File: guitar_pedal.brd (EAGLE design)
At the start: 100 x 80 mm, 89 parts, among them P1 RM-065, P2 RM-065, P3 RM-065, U1 LM324N, U2 LM324N, U3 LM386N-3, U4 LM386N-3, U5 LM386N-3

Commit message: Finished organizing sheets
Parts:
- moved R18 63.5 mm to (-80.0, 48.3)
- moved JP10 62.7 mm to (-20.3, 78.7)
- moved JP4 60.0 mm to (-17.8, 83.8)
- moved R22 48.9 mm to (-26.7, 61.0)
- moved R23 48.9 mm to (-31.8, 61.0)
- moved R20 48.9 mm to (-16.5, 61.0)
- moved R21 48.9 mm to (-21.6, 61.0)
- moved C13 44.5 mm to (-16.5, 48.3)
- moved C16 44.5 mm to (-22.9, 48.3)
- moved C21 44.5 mm to (-35.6, 48.3)
- moved C19 44.5 mm to (-29.2, 48.3)
- moved R3 41.3 mm to (-31.8, 67.3)
- moved R4 41.3 mm to (-36.8, 67.3)
- moved U3 40.6 mm to (-71.1, 6.35)
- moved U1 40.2 mm to (-34.3, 6.35)
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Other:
- board size 100 x 80 mm -> 160 x 100 mm

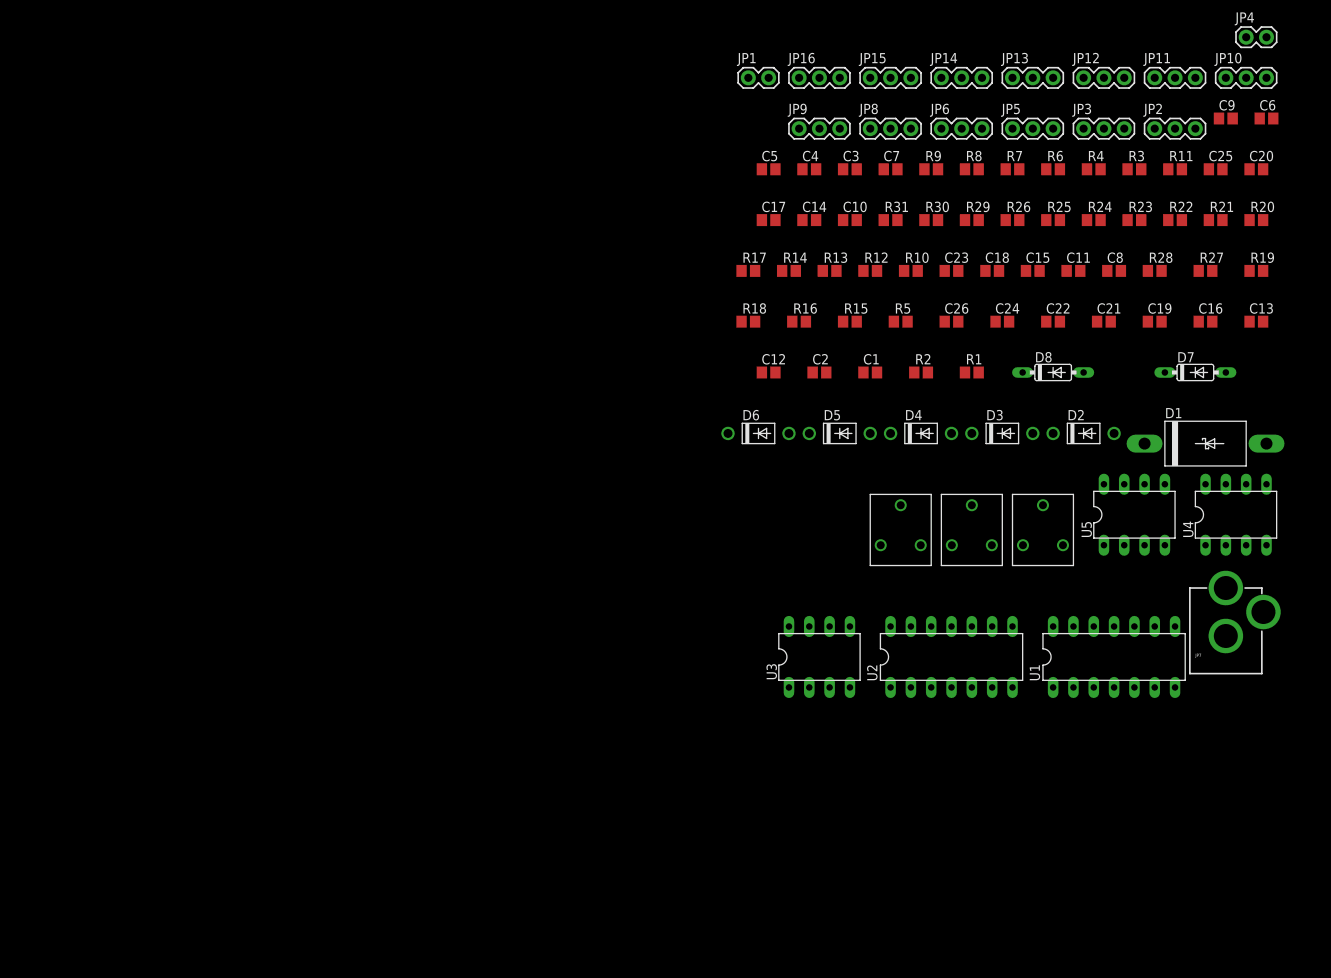
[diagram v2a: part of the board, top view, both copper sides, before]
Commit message: editted schematic to orgainize and fix mistakes.
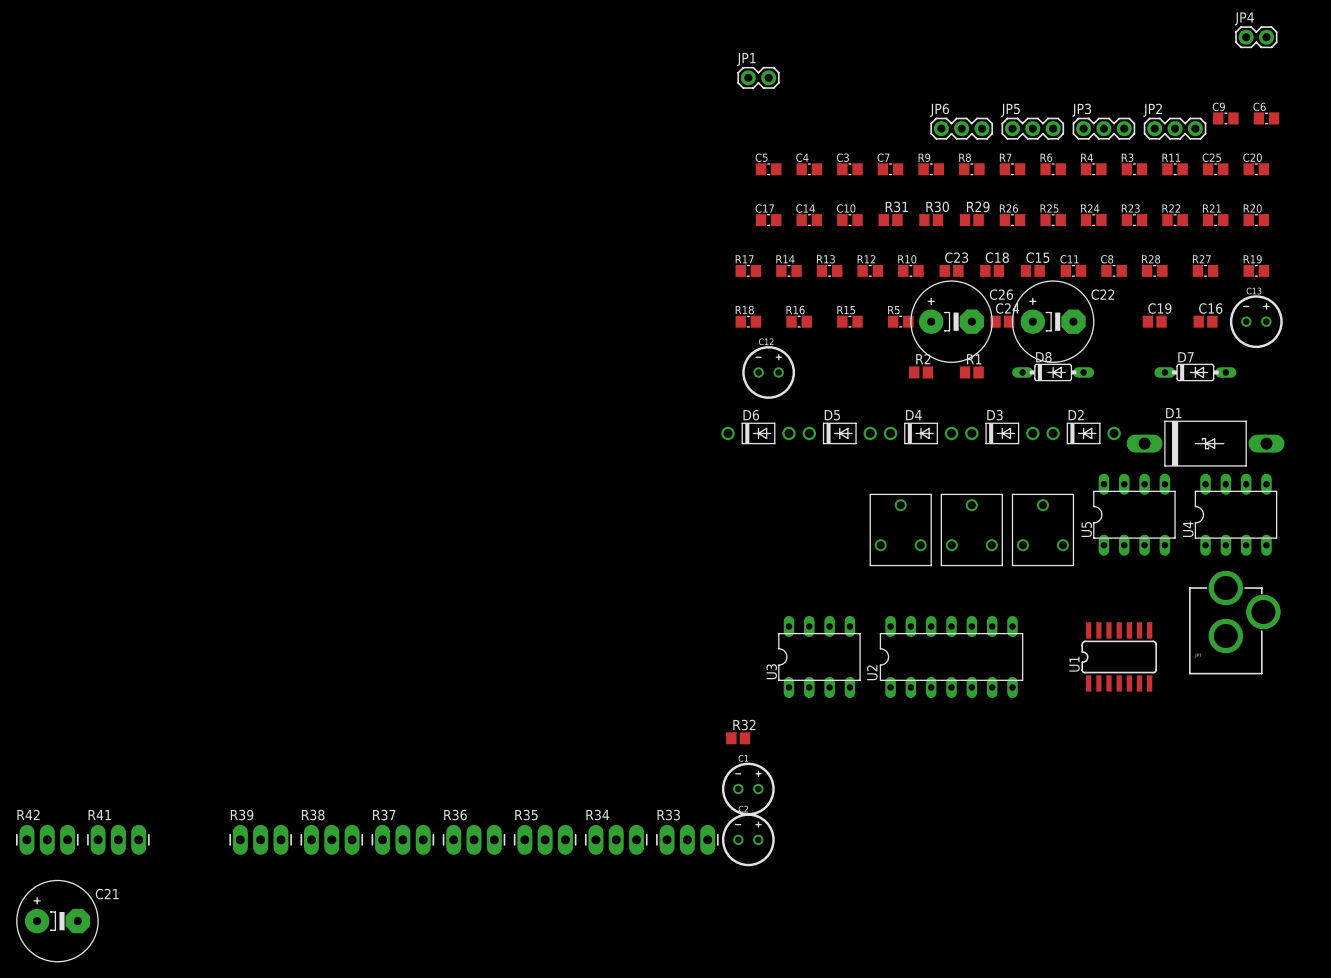
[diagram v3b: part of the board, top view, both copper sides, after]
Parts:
- removed JP10, JP11, JP12, JP13, JP14, JP15, JP16, JP8, JP9: (no value), SparkFun-Connectors:1X03
- added R32: 1A PTC, resistor:R0805
- added R33, R34, R36, R37, R38, R39, R41: 100k, aarons:1X03_LONGPADS
- added R35: (no value), aarons:1X03_LONGPADS
- added R42: 500k, aarons:1X03_LONGPADS
- C1, C12, C13, C2: value 100u -> 100uF 35v; device resistor:C0805 -> Luke:CAN_6MM
- C10, C11, C17, C20, C25, C3, C4, C5, C6, C7, C8, C9: device resistor:C0805 -> Luke:C0805
- C14: value 4u -> 4uF; device resistor:C0805 -> Luke:C0805
- C21, C22, C26: value 330u -> 470uF; device resistor:C0805 -> Luke:CAN01
- C24: value 250u -> 250uF 50v
- D2: value 1N4728 -> 1n4739
- R10: value 3k -> 3.3k; device resistor:R0805 -> Luke:C0805
- R11, R12, R13: value 3k -> 10k; device resistor:R0805 -> Luke:C0805
- R14, R15, R16, R17, R18, R19, R20, R21, R22, R23, R24, R25, R26, R27, R28, R3, R4, R5, R6, R7, R8, R9: device resistor:R0805 -> Luke:C0805
- U1: value LM324N -> LM324NSOIC-14; device aarons:DIL14 -> aarons:SOIC-14
- moved C21 150.8 mm to (-166.4, -26.7)
- moved C2 59.1 mm to (-80.0, -16.5)
- moved C1 54.3 mm to (-80.0, -10.2)
- moved U1 1.27 mm to (-33.0, 6.35)
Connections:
- removed net N$24: C13.1, R22.2, R23.1, U2.4
- removed net N$30: C20.1
- removed net N$37: C25.1
- new net N$32: D1.C, R32.2
- net +9V: now also C1.P+, C2.P+, C21.+, C22.+, C26.+, R32.1; no longer C1.1, C2.1, C21.1, C22.1, C26.1, D1.C
- net AMP_1: now also R33.2; no longer JP8.1
- net AMP_2: now also R34.2; no longer JP9.2, JP9.3
- net AMP_3: now also R35.2; no longer JP10.2
- net AUDIO_IN_L: now also P3.3; no longer P3.1
- net AUDIO_IN_R: now also P2.3; no longer P2.1
- net GND: now also C1.P-, C12.P-, C13.P-, C2.P-, C21.-, C22.-, C26.-, P1.1, P2.1, P3.1, R36.1, R37.1, R38.1; no longer C1.2, C12.2, C13.2, C2.2, C21.2, C22.2, C26.2, JP14.3, JP15.3, JP16.3, U2.14, U2.7, U2.8
- net GTR_IN: now also P1.3; no longer P1.1
- net N$10: now also R41.1; no longer JP12.1
- net N$11: now also R42.1; no longer JP13.1
- net N$13: now also R42.2; no longer JP13.2
- net N$15: now also R39.3; no longer JP11.3
- net N$16: now also R41.3; no longer JP12.3
- net N$17: now also R42.3; no longer JP13.3
- net N$18: now also R39.2; no longer JP11.2
- net N$19: now also R41.2; no longer JP12.2
- net N$2: now also C5.1; no longer P1.2, P3.2
- net N$23: now also R38.2; no longer JP14.2
- net N$26: now also C12.P+; no longer C12.1
- net N$27: now also C20.1
- net N$31: now also R37.2; no longer JP15.2
- net N$35: now also C25.1
- net N$38: now also R36.2; no longer JP16.2
- net N$4: now also P1.2; no longer P1.3
- net N$5: now also C13.P+, R22.2, R23.1, U2.4; no longer C5.1, P2.3
- net N$6: now also P3.2; no longer P3.3
- net N$9: now also R39.1; no longer JP11.1
- net OUT_1: now also R33.1; no longer JP8.2
- net OUT_2: now also R34.1; no longer JP9.1
- net OUT_3: now also R35.3; no longer JP10.3
- net PWR_AMP: now also R36.3, R37.3, R38.3; no longer JP14.1, JP15.1, JP16.1

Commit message: finished schematic changes
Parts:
- removed R32: 1A PTC, resistor:R0805
- added C27, C28, C29, C30, C31, C32, C33: 1uF, Luke:C0805
- added F1: PTCBELFUSE_1206, Luke:1206_PTC
- C15, C18, C23: value .05u -> 47nF; device resistor:C0805 -> Luke:C0805
- C16, C19, C24: device resistor:C0805 -> Luke:CAN01
- D3, D4, D5, D6: value 1N4728 -> 1N4739
- R29, R30, R31: device resistor:R0805 -> Luke:C0805
- R35: value (none) -> 100k
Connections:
- new net N$24: C4.2, D4.C, R4.2
- new net N$30: C6.2, D6.C, R9.2
- new net N$33: C5.2, D5.C, R8.2
- new net N$37: C3.2, D3.C, R3.2
- net +9V: now also C27.1, C28.1, C31.1, C32.1, C33.1, F1.C; no longer R32.1
- net AMP_1: no longer C3.2, C4.2, C5.2, C6.2, D3.C, D4.C, D5.C, D6.C, R3.2, R4.2, R8.2, R9.2
- net AUDIO_OUT: now also C19.-; no longer C19.2
- net GND: now also C27.2, C28.2, C29.2, C30.2, C31.2, C32.2, C33.2
- net GTR_OUT: now also C24.-; no longer C24.2
- net N$25: now also C19.+; no longer C19.1
- net N$32: now also F1.A; no longer R32.2
- net N$34: now also C24.+; no longer C24.1
- net N$5: now also C29.1, C30.1
- net N$8: now also C16.+; no longer C16.1
- net XLR_OUT: now also C16.-; no longer C16.2

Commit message: Started layout. Placed output components.
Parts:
- U2: value LM324N -> LM324NSOIC-14; device aarons:DIL14 -> aarons:SOIC-14
- moved R42 263.5 mm to (80.0, 66.0), turned to 270 degrees
- moved C29 247.6 mm to (43.2, 63.5)
- moved R41 244.4 mm to (67.3, 69.8), turned to 180 degrees
- moved R39 234.9 mm to (80.0, 55.9), turned to 270 degrees
- moved R38 191.0 mm to (49.5, 34.3), turned to 90 degrees
- moved R37 178.8 mm to (49.5, 19.1), turned to 90 degrees
- moved R36 167.6 mm to (49.5, 3.81), turned to 90 degrees
- moved R14 148.6 mm to (73.7, 54.6), turned to 270 degrees
- moved R16 148.4 mm to (73.7, 66.0)
- moved R18 145.1 mm to (64.8, 58.4), turned to 180 degrees
- moved R17 144.8 mm to (64.8, 53.3), turned to 180 degrees
- moved R15 137.0 mm to (68.6, 66.0), turned to 180 degrees
- moved C17 137.0 mm to (57.1, 35.6), turned to 180 degrees
- moved U3 134.7 mm to (58.4, 43.2)
- moved C7 132.8 mm to (69.8, 53.3), turned to 180 degrees
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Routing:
- added copper zone on layer 1, net GND
- added copper zone on layer 16, net GND
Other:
- board size 160 x 100 mm -> 76.2 x 76.2 mm

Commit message: Finished laying out the components.
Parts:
- added C34: 1uF, Luke:C0805
- R1, R2: device resistor:R0805 -> Luke:C0805
- moved C27 258.8 mm to (64.8, 49.5)
- moved C30 258.1 mm to (48.3, 72.4), turned to 90 degrees
- moved C28 251.4 mm to (61.0, 34.3)
- moved C31 250.2 mm to (61.0, 19.1)
- moved C32 224.2 mm to (26.7, 32.4), turned to 180 degrees
- moved C21 218.1 mm to (40.6, 41.9), turned to 180 degrees
- moved C33 209.6 mm to (12.1, 25.4), turned to 180 degrees
- moved F1 194.9 mm to (8.89, 47.0)
- moved R35 139.6 mm to (26.7, 20.3), flipped to the bottom, turned to 270 degrees
- moved R34 133.8 mm to (26.7, 29.2), flipped to the bottom, turned to 270 degrees
- moved R31 133.0 mm to (64.8, 21.6), turned to 90 degrees
- moved R33 127.9 mm to (26.7, 35.6), flipped to the bottom, turned to 90 degrees
- moved C23 124.6 mm to (64.8, 16.5), turned to 90 degrees
- moved R30 124.3 mm to (64.8, 36.8), turned to 90 degrees
- moved R13 114.6 mm to (41.9, 26.7), turned to 90 degrees
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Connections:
- net 4.5: now also C34.1
- net AMP_1: now also R33.1; no longer R33.2
- net AMP_2: now also R34.1; no longer R34.2
- net AUDIO_IN_L: now also P3.1; no longer P3.3
- net GND: now also C34.2, P3.3; no longer P3.1
- net OUT_1: now also R33.2; no longer R33.1
- net OUT_2: now also R34.2; no longer R34.1
